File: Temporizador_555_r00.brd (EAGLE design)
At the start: 49.7 x 49.8 mm, 9 parts, among them IC1 LM555

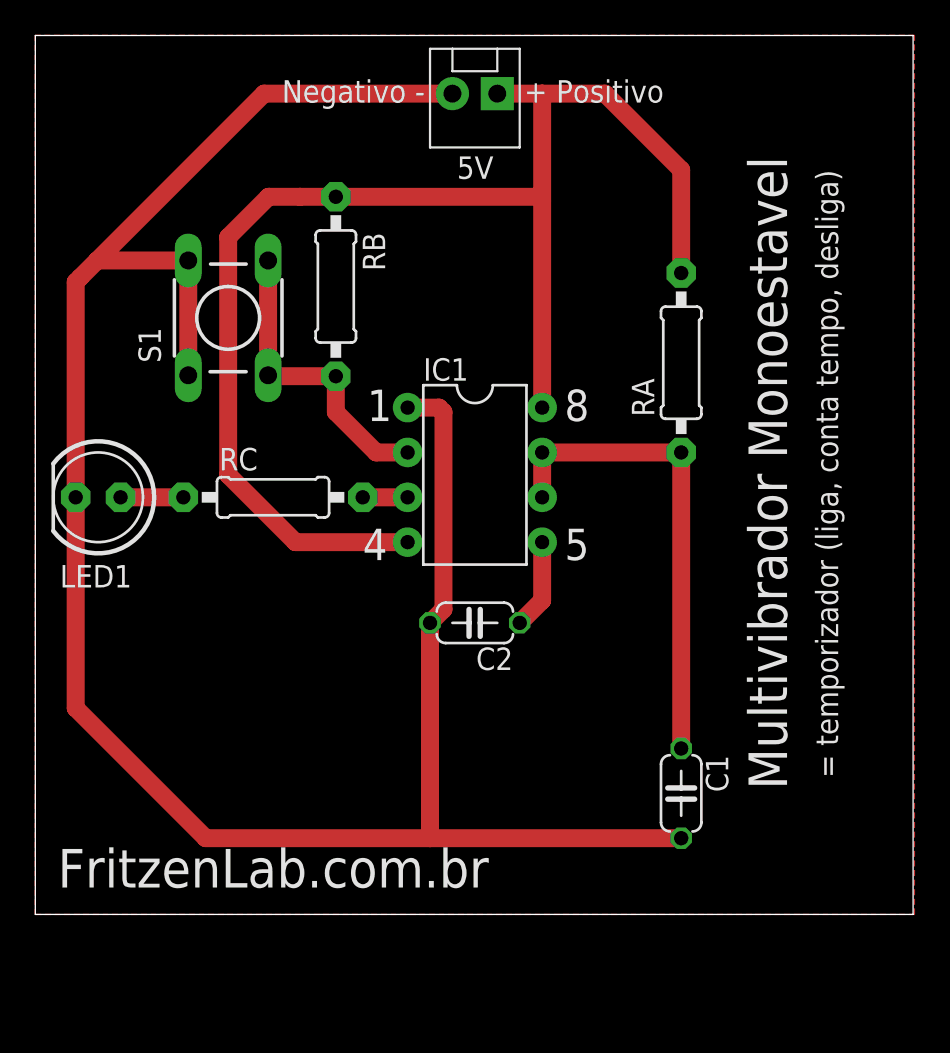
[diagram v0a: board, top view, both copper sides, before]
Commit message: Primeira revisao (r00) e arquivos para fabricacao
Primeira revisao (estética e troca do conector da fonte por um KRE 5mm).
Gerados Gerber para fabricaçao da PCI
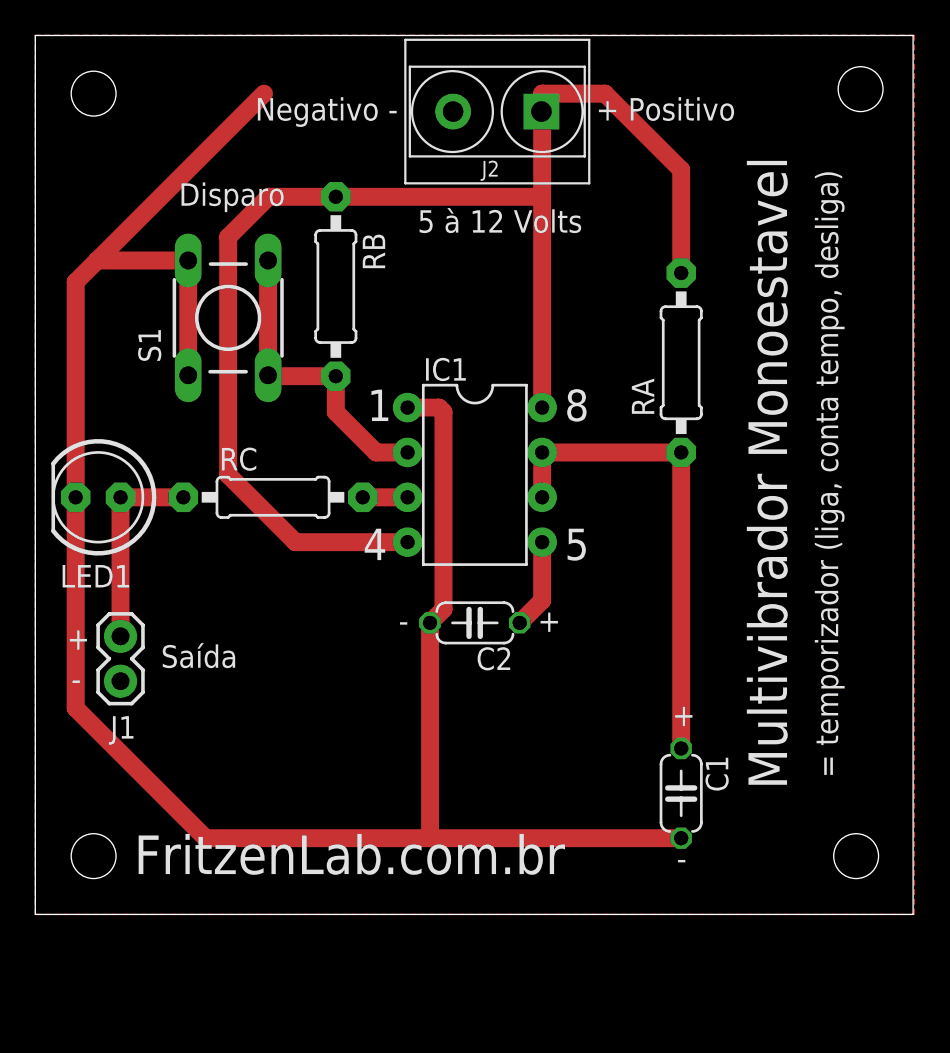
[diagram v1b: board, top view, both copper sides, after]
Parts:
- added J2: GSL009-5.0-02P-12, Seeed-OPL-Connector:H2-5.0-10.5X8.0MM
- J1: device SparkFun-Connectors:MOLEX-1X2 -> SparkFun-Connectors:1X02
- moved J1 37.4 mm to (4.83, 15.7), turned to 270 degrees
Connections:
- net GND: now also J2.2
- net N$3: now also J1.1
- net VCC: now also J2.1; no longer J1.1
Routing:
- net GND: track 125.5 -> 114.8 mm
- net N$3: track 3.56 -> 11.4 mm
- net VCC: track 79.9 -> 77.4 mm
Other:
- board text added: "+"
- board text added: "-"
- board text added: "5 à 12 Volts"
- board text added: "Disparo"
- board text added: "Saída"
- board text removed: "5V"
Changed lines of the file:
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@@
 <layer number="43" name="vRestrict" color="2" fill="10" visible="yes" active="yes"/>
 <layer number="44" name="Drills" color="7" fill="1" visible="no" active="yes"/>
-<layer number="45" name="Holes" color="7" fill="1" visible="no" active="yes"/>
+<layer number="45" name="Holes" color="7" fill="1" visible="yes" active="yes"/>
 <layer number="46" name="Milling" color="3" fill="1" visible="no" active="yes"/>
 <layer number="47" name="Measures" color="7" fill="1" visible="no" active="yes"/>
@@
 <layer number="115" name="ReferenceISLANDS" color="7" fill="1" visible="yes" active="yes"/>
 <layer number="116" name="Patch_BOT" color="9" fill="4" visible="no" active="yes"/>
+<layer number="117" name="BACKMAAT1" color="7" fill="1" visible="no" active="no"/>
 <layer number="118" name="Rect_Pads" color="7" fill="1" visible="no" active="no"/>
+<layer number="119" name="KAP_TEKEN" color="7" fill="1" visible="no" active="no"/>
+<layer number="120" name="KAP_MAAT1" color="7" fill="1" visible="no" active="no"/>
 <layer number="121" name="_tsilk" color="7" fill="1" visible="no" active="yes"/>
 <layer number="122" name="_bsilk" color="7" fill="1" visible="no" active="yes"/>
@@
 <layer number="128" name="_bValues" color="7" fill="1" visible="no" active="yes"/>
 <layer number="129" name="Mask" color="7" fill="1" visible="yes" active="yes"/>
+<layer number="130" name="SMDSTROOK" color="7" fill="1" visible="no" active="no"/>
 <layer number="131" name="tAdjust" color="7" fill="1" visible="no" active="yes"/>
 <layer number="132" name="bAdjust" color="7" fill="1" visible="no" active="yes"/>
+<layer number="133" name="bottom_silk" color="7" fill="1" visible="no" active="no"/>
 <layer number="144" name="Drill_legend" color="7" fill="1" visible="no" active="yes"/>
 <layer number="150" name="Notes" color="7" fill="1" visible="no" active="yes"/>
@@
 <text x="40.386" y="42.926" size="2.1844" layer="25" rot="R270">Multivibrador Monoestavel</text>
 <text x="44.196" y="42.164" size="1.27" layer="25" rot="R270">= temporizador (liga, conta tempo, desliga)</text>
-<text x="27.686" y="45.974" size="1.27" layer="25">+ Positivo</text>
-<text x="13.97" y="45.974" size="1.27" layer="25">Negativo -</text>
-<text x="23.876" y="41.656" size="1.27" layer="25">5V</text>
-<text x="1.27" y="1.524" size="2.1844" layer="25">FritzenLab.com.br</text>
+<text x="31.75" y="44.958" size="1.27" layer="25">+ Positivo</text>
+<text x="12.446" y="44.958" size="1.27" layer="25">Negativo -</text>
+<text x="30.988" y="39.878" size="1.27" layer="25" rot="R180">5 à 12 Volts</text>
+<text x="5.588" y="2.286" size="2.1844" layer="25">FritzenLab.com.br</text>
 <text x="18.796" y="27.94" size="1.778" layer="25">1</text>
 <text x="18.542" y="20.066" size="1.778" layer="25">4</text>
 <text x="29.972" y="20.066" size="1.778" layer="25">5</text>
 <text x="29.972" y="27.94" size="1.778" layer="25">8</text>
+<hole x="3.302" y="3.302" drill="2.54"/>
+<hole x="46.482" y="3.302" drill="2.54"/>
+<hole x="3.302" y="46.482" drill="2.54"/>
+<hole x="46.736" y="46.736" drill="2.54"/>
+<text x="2.032" y="12.7" size="1.27" layer="25">-</text>
+<text x="36.322" y="2.54" size="1.27" layer="25">-</text>
+<text x="20.574" y="16.002" size="1.27" layer="25">-</text>
+<text x="1.778" y="14.986" size="1.27" layer="25">+</text>
+<text x="28.448" y="16.002" size="1.27" layer="25">+</text>
+<text x="36.068" y="10.668" size="1.27" layer="25">+</text>
+<text x="8.128" y="40.132" size="1.27" layer="25">Disparo</text>
+<text x="7.112" y="13.97" size="1.27" layer="25">Saída</text>
 </plain>
 <attributes>
@@
 </class>
 </classes>
-<designrules name="Elecrow_2-layer_PCB_eagle_rule">
+<designrules name="Elecrow_2-layer_PCB_eagle_rule *">
 <description language="de">&lt;b&gt;EAGLE Design Rules&lt;/b&gt;
 &lt;p&gt;
@@
 <param name="mtCopper" value="0.035mm 0.035mm 0.035mm 0.035mm 0.035mm 0.035mm 0.035mm 0.035mm 0.035mm 0.035mm 0.035mm 0.035mm 0.035mm 0.035mm 0.035mm 0.035mm"/>
 <param name="mtIsolate" value="1.6mm 1.2mm 0.2mm 0.15mm 0.2mm 0.15mm 0.2mm 0.15mm 0.2mm 0.15mm 0.2mm 0.15mm 0.2mm 0.15mm 0.2mm"/>
-<param name="mdWireWire" value="6mil"/>
-<param name="mdWirePad" value="6mil"/>
-<param name="mdWireVia" value="6mil"/>
-<param name="mdPadPad" value="6mil"/>
-<param name="mdPadVia" value="6mil"/>
-<param name="mdViaVia" value="8mil"/>
+<param name="mdWireWire" value="10mil"/>
+<param name="mdWirePad" value="10mil"/>
+<param name="mdWireVia" value="10mil"/>
+<param name="mdPadPad" value="10mil"/>
+<param name="mdPadVia" value="10mil"/>
+<param name="mdViaVia" value="10mil"/>
 <param name="mdSmdPad" value="0mil"/>
 <param name="mdSmdVia" value="0mil"/>
@@
 <param name="mdViaViaSameLayer" value="8mil"/>
 <param name="mnLayersViaInSmd" value="2"/>
-<param name="mdCopperDimension" value="20mil"/>
+<param name="mdCopperDimension" value="10mil"/>
 <param name="mdDrill" value="10mil"/>
 <param name="mdSmdStop" value="0mil"/>
@@
 <attribute name="VALUE" x="27.432" y="33.909" size="1.27" layer="27" ratio="10" rot="R180"/>
 </element>
-<element name="J1" library="SparkFun-Connectors" package="MOLEX-1X2" value="" x="26.162" y="46.482" rot="R180"/>
 <element name="LED1" library="adafruit" package="LED5MM" value="Vermelho" x="3.556" y="23.622" smashed="yes" rot="R180">
 <attribute name="NAME" x="5.461" y="19.7866" size="1.27" layer="25" ratio="10" rot="R180"/>
@@
 <element name="S1" library="GeekAmmo" package="TAC-SWITCH-PTH" value="TACTILE-SWITCH-PTH" x="10.922" y="33.782" smashed="yes" rot="R90">
 <attribute name="NAME" x="7.112" y="31.242" size="1.27" layer="25" ratio="10" rot="R90"/>
+</element>
+<element name="J1" library="SparkFun-Connectors" package="1X02" value="" x="4.826" y="15.748" smashed="yes" rot="R270">
+<attribute name="NAME" x="4.2418" y="9.9568" size="1.27" layer="25" ratio="10"/>
+<attribute name="VALUE" x="1.651" y="17.018" size="1.27" layer="27" rot="R270"/>
+</element>
+<element name="J2" library="Seeed-OPL-Connector" package="H2-5.0-10.5X8.0MM" value="GSL009-5.0-02P-12" x="26.162" y="45.466" smashed="yes" rot="R270">
+<attribute name="MPN" value="GSL009-5.0-02P-12" x="26.162" y="45.466" size="1.778" layer="27" rot="R270" display="off"/>
+<attribute name="NAME" x="25.273" y="41.783" size="0.889" layer="25" ratio="11"/>
 </element>
 </elements>
@@
 <contactref element="IC1" pad="4"/>
 <contactref element="RA" pad="2"/>
-<contactref element="J1" pad="1"/>
-<wire x1="26.162" y1="46.482" x2="28.702" y2="46.482" width="1.016" layer="1"/>
 <wire x1="28.702" y1="46.482" x2="32.258" y2="46.482" width="1.016" layer="1"/>
 <wire x1="32.258" y1="46.482" x2="36.576" y2="42.164" width="1.016" layer="1"/>
 <wire x1="36.576" y1="42.164" x2="36.576" y2="36.322" width="1.016" layer="1"/>
 <wire x1="28.702" y1="28.702" x2="28.702" y2="40.386" width="1.016" layer="1"/>
-<wire x1="28.702" y1="40.386" x2="28.702" y2="46.482" width="1.016" layer="1"/>
+<wire x1="28.702" y1="40.386" x2="28.702" y2="45.466" width="1.016" layer="1"/>
+<wire x1="28.702" y1="45.72" x2="28.702" y2="46.482" width="1.016" layer="1"/>
 <wire x1="21.082" y1="21.082" x2="14.732" y2="21.082" width="1.016" layer="1"/>
 <contactref element="RB" pad="1"/>
@@
 <wire x1="10.922" y1="24.892" x2="10.922" y2="38.354" width="1.016" layer="1"/>
 <wire x1="10.922" y1="38.354" x2="13.208" y2="40.64" width="1.016" layer="1"/>
-<wire x1="13.208" y1="40.64" x2="14.986" y2="40.64" width="1.016" layer="1"/>
 <wire x1="17.018" y1="40.64" x2="28.448" y2="40.64" width="1.016" layer="1"/>
 <wire x1="28.448" y1="40.64" x2="28.702" y2="40.386" width="1.016" layer="1"/>
-<wire x1="17.018" y1="40.64" x2="14.986" y2="40.64" width="1.016" layer="1"/>
+<wire x1="17.018" y1="40.64" x2="13.208" y2="40.64" width="1.016" layer="1"/>
+<contactref element="J2" pad="1"/>
+<wire x1="28.662" y1="45.466" x2="28.702" y2="45.466" width="1.016" layer="1"/>
+<wire x1="28.702" y1="45.466" x2="28.702" y2="45.72" width="1.016" layer="1"/>
 </signal>
 <signal name="N$2">
@@
 <contactref element="LED1" pad="K"/>
 <contactref element="C1" pad="2"/>
-<contactref element="J1" pad="2"/>
-<wire x1="23.622" y1="46.482" x2="12.954" y2="46.482" width="1.016" layer="1"/>
 <wire x1="12.954" y1="46.482" x2="3.5052" y2="37.0332" width="1.016" layer="1"/>
-<wire x1="2.54" y1="36.068" x2="2.286" y2="35.814" width="1.016" layer="1"/>
 <wire x1="2.286" y1="35.814" x2="2.286" y2="23.622" width="1.016" layer="1"/>
 <wire x1="36.576" y1="4.318" x2="22.352" y2="4.318" width="1.016" layer="1"/>
@@
 <wire x1="8.6614" y1="37.0332" x2="8.6614" y2="30.5308" width="1.016" layer="1"/>
 <wire x1="8.6614" y1="37.0332" x2="3.5052" y2="37.0332" width="1.016" layer="1"/>
-<wire x1="3.5052" y1="37.0332" x2="2.54" y2="36.068" width="1.016" layer="1"/>
+<wire x1="3.5052" y1="37.0332" x2="2.286" y2="35.814" width="1.016" layer="1"/>
+<contactref element="J1" pad="2"/>
+<contactref element="J2" pad="2"/>
 </signal>
 <signal name="N$3">
@@
 <contactref element="RC" pad="1"/>
 <wire x1="8.382" y1="23.622" x2="4.826" y2="23.622" width="1.016" layer="1"/>
+<contactref element="J1" pad="1"/>
+<wire x1="4.826" y1="23.622" x2="4.826" y2="15.748" width="1.016" layer="1"/>
 </signal>
 <signal name="N$4">

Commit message: Upload de arquivos atuais que foram para produção
Upload de arquivos atuais que foram para produção
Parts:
- C1: value 0.1uF -> 10uF
- RA: value 6.8k -> 470k
- RB, RC: value 680 -> 1k
- moved J2 0.57 mm to (26.4, 45.0)
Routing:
- net GND: track 114.8 -> 125.7 mm
- net VCC: track 77.4 -> 77.9 mm
- added copper zone on layer 16, net GND
- removed copper zone on layer 1, net GND
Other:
- board size 49.7 x 49.8 mm -> 48.7 x 49.8 mm
